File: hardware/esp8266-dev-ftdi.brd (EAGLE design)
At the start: 100 x 80 mm, 28 parts, among them CON1 USBMICRO-NO_CENTER, IC2 3V3

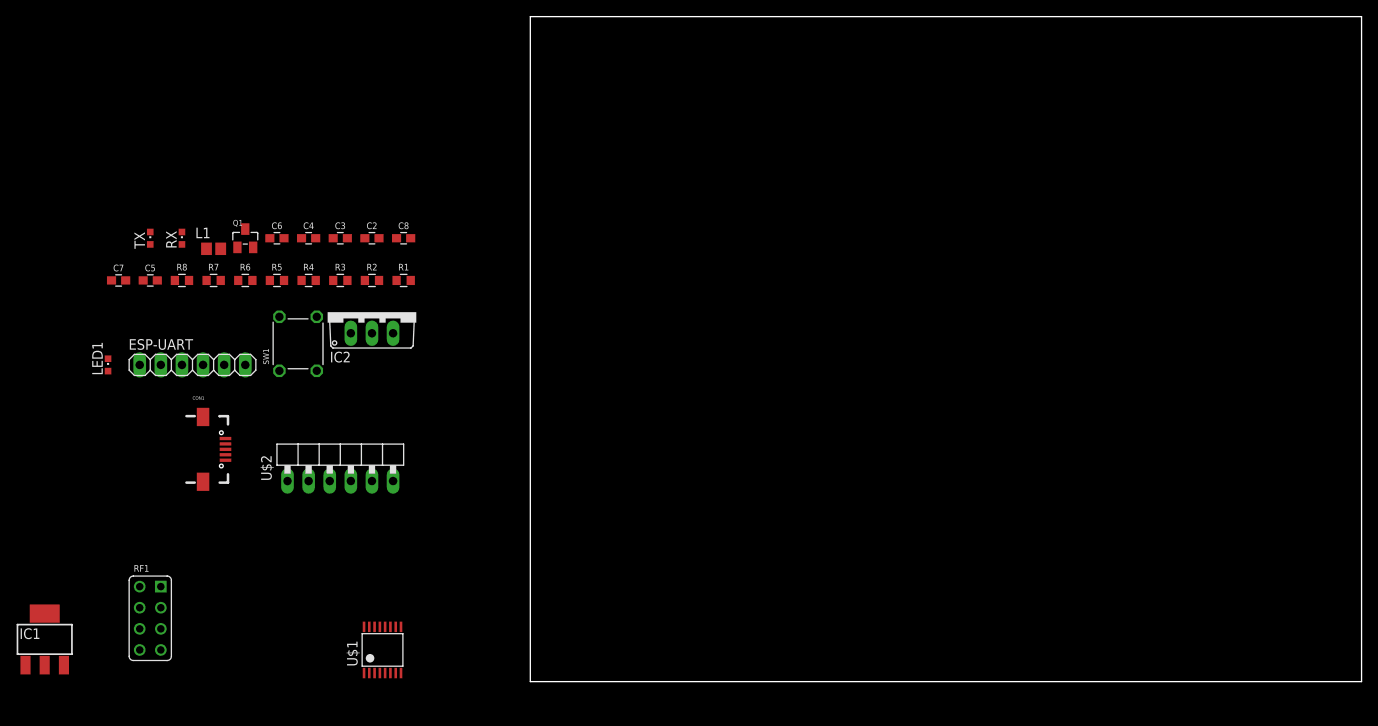
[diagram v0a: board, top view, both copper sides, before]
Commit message: Added LEDs
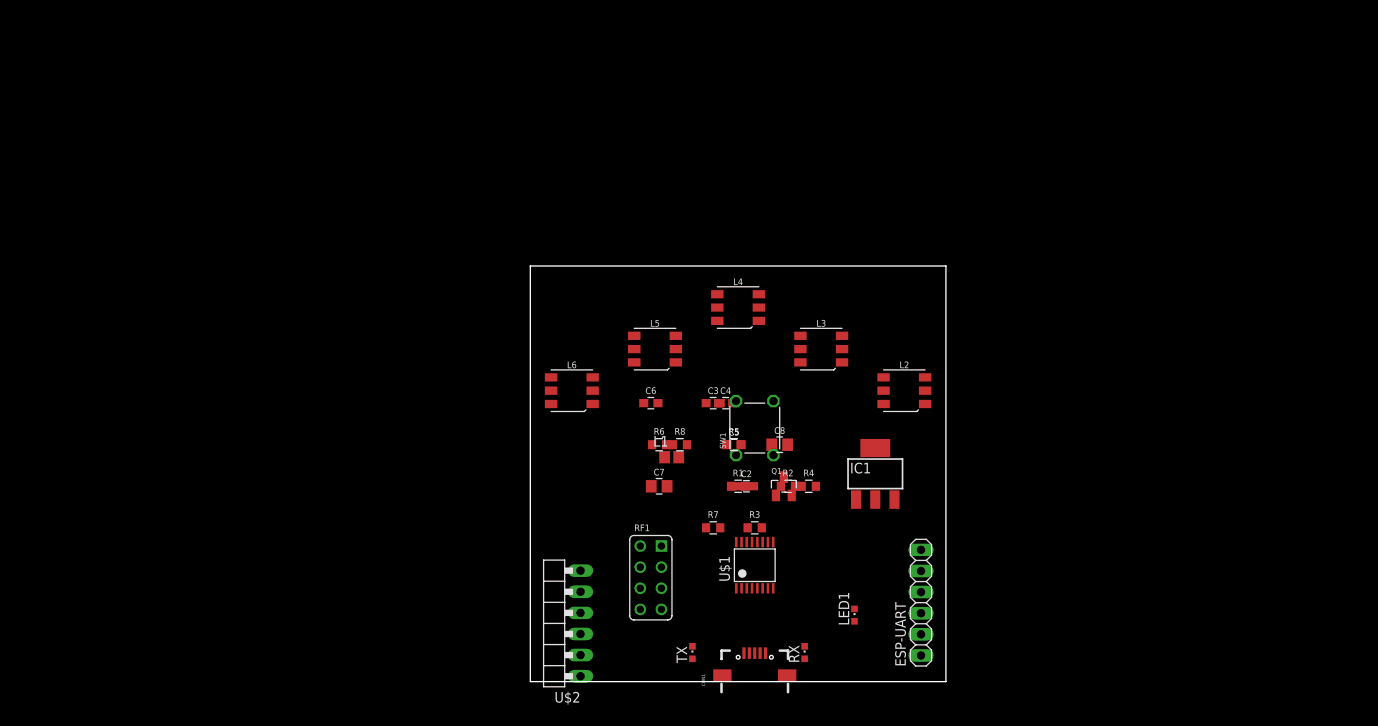
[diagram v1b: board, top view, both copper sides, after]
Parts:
- removed IC2: 3V3, p.peter-regulators:TO220V
- added L2, L3, L4, L5, L6: WS2812S, p.peter-leds:CHIP-5050
- C7: value 330n -> 10u; device p.peter-rcl:C0603 -> p.peter-rcl:C0805
- C8: value 100n -> 22u; device p.peter-rcl:C0603 -> p.peter-rcl:C0805
- moved IC1 101.9 mm to (41.5, 25.0)
- moved LED1 94.7 mm to (39.0, 8.00)
- moved ESP-UART 92.2 mm to (47.0, 9.50), turned to 90 degrees
- moved RX 90.0 mm to (33.0, 3.50)
- moved TX 82.1 mm to (19.5, 3.50)
- moved C5 72.9 mm to (24.5, 28.5)
- moved Q1 71.3 mm to (30.5, 23.5)
- moved CON1 70.1 mm to (27.0, 2.00), turned to 90 degrees
- moved C7 69.6 mm to (15.5, 23.5)
- moved R7 67.1 mm to (22.0, 18.5)
- moved R4 65.1 mm to (33.5, 23.5)
- moved R8 63.1 mm to (18.0, 28.5)
- moved L1 60.5 mm to (17.0, 27.0)
- moved RF1 60.4 mm to (14.5, 12.5)
- moved R5 58.4 mm to (24.5, 28.5)
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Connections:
- net +3V3: now also IC1.2, IC1.4; no longer IC2.3
- net +5V: now also IC1.3; no longer IC2.1
- net GND: now also IC1.1; no longer IC2.2
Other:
- board size 100 x 80 mm -> 50 x 50 mm

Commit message: schematic mostly done
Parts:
- removed ESP-UART: (no value), p.peter-connectors:PINHEADER-100MIL-1X6
- removed L2, L3, L4, L5, L6: WS2812S, p.peter-leds:CHIP-5050
- removed RX, TX: (no value), p.peter-leds:CHIPLED_0603
- added F1: 500mA, p.peter-regulators:SMD-FUSE-0805
- added LED-RX, LED-TX: (no value), p.peter-leds:CHIPLED_0805
- added LED2, LED3, LED4, LED5, LED6: (no value), p.peter-leds:CHIP-5050-4_PIN
- added R10, R9: 2k, p.peter-rcl:R0603
- added SJ1: (no value), jumper:SJ
- added SJ2: (no value), jumper:SJ_2
- added SW2, SW3, SW4: (no value), p.peter-passives:SWITCH-GENERIC-2_PIN
- L1: value (none) -> 875-MI0805K601R-10; device dp_devices:FB603 -> p.peter-passives:R0805
- LED1: device p.peter-leds:CHIPLED_0603 -> p.peter-leds:CHIPLED_0805
- moved U$2 20.0 mm to (4.00, 27.0)
- moved RF1 9.19 mm to (18.0, 21.0), turned to 45 degrees
- moved C4 0.71 mm to (24.0, 34.0)
- moved C5 0.71 mm to (25.0, 29.0)
- moved C6 0.71 mm to (15.0, 34.0)
- moved C7 0.71 mm to (16.0, 24.0)
- moved Q1 0.71 mm to (31.0, 24.0)
- moved R4 0.71 mm to (34.0, 24.0)
- moved R5 0.71 mm to (25.0, 29.0)
- moved R6 0.71 mm to (16.0, 29.0)
- moved C2 0.50 mm to (26.0, 24.0)
- moved C3 0.50 mm to (22.0, 34.0)
- moved C8 0.50 mm to (30.0, 29.0)
- moved IC1 0.50 mm to (42.0, 25.0)
- moved R1 0.50 mm to (25.0, 24.0)
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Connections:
- new net N$12: LED2.P$2, LED3.P$4
- new net N$15: LED3.P$2, LED4.P$4
- new net N$16: LED4.P$2, LED5.P$4
- new net N$17: LED5.P$2, LED6.P$4
- new net N$18: CON1.VUSB, F1.2, SJ1.2
- new net N$20: R9.2, SW3.P$1
- new net N$21: R10.2, SW4.P$1
- new net VCCIO: SJ2.2, U$1.3, U$2.3
- net +3V3: now also SJ2.3; no longer ESP-UART.3, U$1.3
- net +5V: now also LED2.P$1, LED3.P$1, LED4.P$1, LED5.P$1, LED6.P$1, SJ2.1; no longer U$2.3
- net /SLEEP: now also U$2.6
- net CTS: now also U$2.2
- net GND: now also LED-RX.C, LED-TX.C, LED2.P$3, LED3.P$3, LED4.P$3, LED5.P$3, LED6.P$3, R10.1, R9.1, SW2.P$1; no longer ESP-UART.1, RX.C, TX.C
- net IO2: now also LED2.P$4
- net N$10: now also SW2.P$2
- net N$2: now also F1.1, SJ1.1; no longer CON1.VUSB
- net N$3: now also LED-TX.A; no longer TX.A
- net N$8: now also LED-RX.A; no longer RX.A
- net RX: now also SW4.P$2; no longer ESP-UART.5
- net TX: now also SW3.P$2; no longer ESP-UART.4

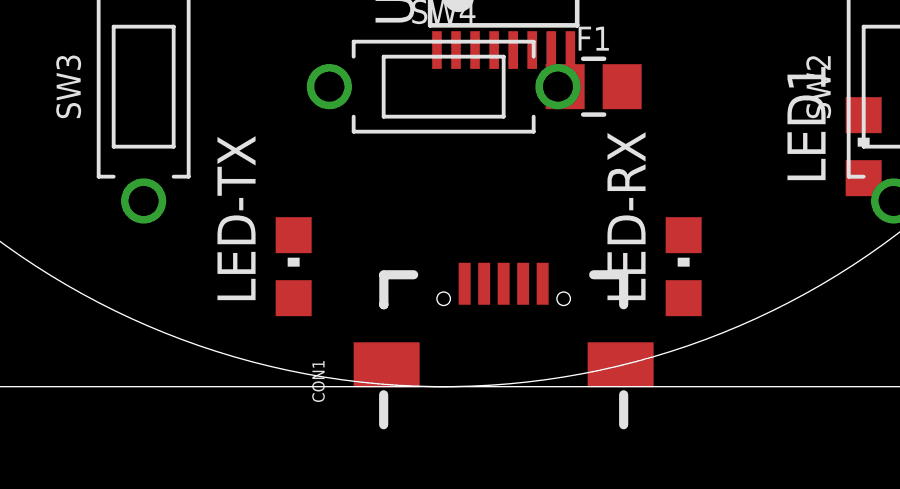
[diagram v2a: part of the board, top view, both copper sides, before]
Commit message: new USB connector with longer pads
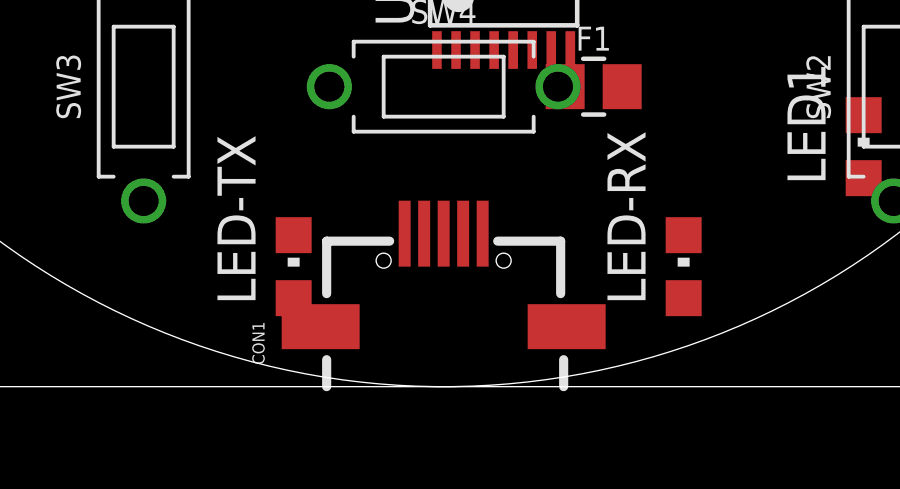
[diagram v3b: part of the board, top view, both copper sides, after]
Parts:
- CON1: value USBMICRO-NO_CENTER -> USBMICRO-NO_CENTER-LONG_PADS; device p.peter-connectors:USB-MICRO-SMD-NO_CENTER -> p.peter-connectors:USB-MICRO-SMD-NO_CENTER-LONG_PADS
- moved CON1 2.00 mm to (25.0, 2.00)
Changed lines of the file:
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@@
 <setting verticaltext="up"/>
 </settings>
-<grid distance="5" unitdist="mm" unit="mm" style="dots" multiple="1" display="no" altdistance="1" altunitdist="mm" altunit="mm"/>
+<grid distance="1" unitdist="mm" unit="mm" style="dots" multiple="1" display="yes" altdistance="0.1" altunitdist="mm" altunit="mm"/>
 <layers>
 <layer number="1" name="Top" color="4" fill="1" visible="yes" active="yes"/>
@@
 <element name="C7" library="p.peter-rcl" package="C0805" value="10u" x="16" y="24"/>
 <element name="C8" library="p.peter-rcl" package="C0805" value="22u" x="30" y="29"/>
-<element name="CON1" library="p.peter-connectors" package="USB-MICRO-SMD-NO_CENTER" value="USBMICRO-NO_CENTER" x="27" y="2" rot="R90"/>
+<element name="CON1" library="p.peter-connectors" package="USB-MICRO-SMD-NO_CENTER-LONG_PADS" value="USBMICRO-NO_CENTER-LONG_PADS" x="25" y="2" rot="R90"/>
 <element name="L1" library="p.peter-passives" package="R0805" value=" 875-MI0805K601R-10" x="17" y="27"/>
 <element name="LED1" library="p.peter-leds" package="CHIPLED_0805" value="" x="39" y="8"/>
@@
 <wire x1="6.54" y1="20.65" x2="7.7" y2="33.4" width="0" layer="19" extent="1-1"/>
 <wire x1="20" y1="5.05" x2="6.54" y2="20.65" width="0" layer="19" extent="1-1"/>
-<wire x1="28.3" y1="3.43" x2="20" y2="5.05" width="0" layer="19" extent="1-1"/>
-<wire x1="33" y1="5.05" x2="28.3" y2="3.43" width="0" layer="19" extent="1-1"/>
-<wire x1="27.317" y1="11.221" x2="28.3" y2="3.43" width="0" layer="19" extent="1-1"/>
+<wire x1="26.3" y1="5.1" x2="20" y2="5.05" width="0" layer="19" extent="1-1"/>
+<wire x1="33" y1="5.05" x2="26.3" y2="5.1" width="0" layer="19" extent="1-1"/>
+<wire x1="27.317" y1="11.221" x2="26.3" y2="5.1" width="0" layer="19" extent="1-1"/>
 <wire x1="26.682" y1="16.779" x2="27.317" y2="11.221" width="0" layer="19" extent="1-1"/>
 <wire x1="26.85" y1="24" x2="26.682" y2="16.779" width="0" layer="19" extent="1-1"/>
@@
 <contactref element="C3" pad="1"/>
 <wire x1="21.15" y1="34" x2="25.85" y2="24" width="0" layer="19" extent="1-1"/>
-<wire x1="26.35" y1="3.43" x2="21.15" y2="34" width="0" layer="19" extent="1-1"/>
+<wire x1="24.35" y1="5.1" x2="21.15" y2="34" width="0" layer="19" extent="1-1"/>
 </signal>
 <signal name="N$5">
@@
 <contactref element="C4" pad="1"/>
 <wire x1="23.15" y1="34" x2="31.85" y2="24" width="0" layer="19" extent="1-1"/>
-<wire x1="27" y1="3.43" x2="23.15" y2="34" width="0" layer="19" extent="1-1"/>
+<wire x1="25" y1="5.1" x2="23.15" y2="34" width="0" layer="19" extent="1-1"/>
 </signal>
 <signal name="TX">
@@
 <contactref element="SJ1" pad="2"/>
 <wire x1="30.95" y1="10" x2="35.762" y2="20" width="0" layer="19" extent="1-1"/>
-<wire x1="25.7" y1="3.43" x2="30.95" y2="10" width="0" layer="19" extent="1-1"/>
+<wire x1="23.7" y1="5.1" x2="30.95" y2="10" width="0" layer="19" extent="1-1"/>
 </signal>
 <signal name="N$20">

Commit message: starting layout
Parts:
- added JP1: (no value), pinhead:2X05
- added R11: 10k, p.peter-rcl:R0603
- added TP1, TP10, TP11, TP2, TP3, TP4, TP5, TP6, TP7, TP8, TP9: TPSQTP15R, testpad:TP15R
- moved SW3 30.9 mm to (43.0, 23.0)
- moved SW1 23.9 mm to (14.0, 11.0)
- moved RF1 14.3 mm to (32.0, 18.0), turned to 135 degrees
- moved U$2 2.24 mm to (3.00, 25.0)
- moved CON1 0.50 mm to (25.0, 2.50)
- flipped C2 to the bottom
- flipped C3 to the bottom
- flipped C4 to the bottom
- flipped C5 to the bottom
- flipped C6 to the bottom
- flipped C7 to the bottom
- flipped C8 to the bottom
- flipped F1 to the bottom
- flipped IC1 to the bottom
- flipped L1 to the bottom
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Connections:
- removed net N$10: Q1.P$3, R6.1, RF1.H_PD, SW2.P$2
- new net RESET: JP1.9, Q1.P$3, R6.1, RF1.H_PD, SW2.P$2, TP5.TP
- net +3V3: now also JP1.3, R11.1, TP10.TP
- net +5V: now also JP1.1, TP9.TP
- net /PWREN: now also TP7.TP
- net /SLEEP: now also TP6.TP
- net CTS: now also TP2.TP
- net GND: now also JP1.4, TP11.TP
- net IO0: now also JP1.6
- net IO16: now also JP1.10
- net IO2: now also JP1.8, R11.2
- net RTS: now also TP1.TP
- net RX: now also JP1.5, TP3.TP
- net TX: now also JP1.7, TP4.TP
- net VCCIO: now also JP1.2, TP8.TP
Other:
- outline, holes or cut-outs redrawn

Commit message: board outline and orga
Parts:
- removed SW4: (no value), p.peter-passives:SWITCH-GENERIC-2_PIN
- added SW-RESET: (no value), p.peter-passives:SWITCH-GENERIC-2_PIN
- moved SW3 36.8 mm to (9.00, 9.00), turned to 315 degrees
- moved JP1 26.2 mm to (46.0, 25.0), flipped to the bottom
- moved SW1 5.39 mm to (16.0, 16.0), turned to 45 degrees
- moved LED2 5.00 mm to (9.00, 38.0), turned to 45 degrees
- moved LED6 5.00 mm to (41.0, 38.0), turned to 315 degrees
- moved LED3 3.16 mm to (16.0, 44.0), turned to 22.5 degrees
- moved LED5 2.24 mm to (34.0, 44.0), turned to 337.5 degrees
- moved LED4 2.00 mm to (25.0, 46.0)
- moved SW2 1.41 mm to (41.0, 9.00), turned to 225 degrees
- moved U$2 1.00 mm to (2.00, 25.0), flipped to the bottom, turned to 270 degrees
- moved RF1 0.42 mm to (31.7, 18.3)
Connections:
- net GND: now also SW-RESET.P$1; no longer SW2.P$1
- net N$20: now also SW2.P$1; no longer SW3.P$1
- net N$21: now also SW3.P$1; no longer SW4.P$1
- net RESET: now also SW-RESET.P$2; no longer SW2.P$2
- net RX: now also SW3.P$2; no longer SW4.P$2
- net TX: now also SW2.P$2; no longer SW3.P$2
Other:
- outline, holes or cut-outs redrawn

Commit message: LED power
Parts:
- removed TP1, TP10, TP11, TP2, TP3, TP4, TP5, TP6, TP7, TP8, TP9: TPSQTP15R, testpad:TP15R
- C2, C3, C4, C5, C6: device p.peter-rcl:C0603 -> p.peter-rcl:C0805
- R1, R10, R11, R2, R3, R4, R5, R6, R7, R8, R9: device p.peter-rcl:R0603 -> p.peter-rcl:R0805
- moved LED-RX 32.6 mm to (9.00, 26.0), flipped to the top, turned to 270 degrees
- moved LED2 32.5 mm to (41.5, 38.5), turned to 315 degrees
- moved LED6 32.5 mm to (8.50, 38.5), turned to 45 degrees
- moved IC1 30.2 mm to (17.0, 8.00), turned to 180 degrees
- moved LED-TX 30.1 mm to (9.00, 32.0), flipped to the top, turned to 90 degrees
- moved R10 28.9 mm to (23.0, 43.0)
- moved SJ2 28.0 mm to (14.0, 43.0)
- moved R9 27.3 mm to (34.0, 42.0)
- moved R7 27.0 mm to (22.0, 46.0)
- moved C8 25.8 mm to (12.4, 10.2), turned to 270 degrees
- moved SW1 25.5 mm to (34.0, 34.0)
- moved R3 25.1 mm to (39.0, 41.0)
- moved R11 24.2 mm to (10.0, 38.0)
- moved R4 22.1 mm to (27.0, 45.0)
- moved SW-RESET 21.2 mm to (18.0, 18.0)
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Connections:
- net +3V3: no longer TP10.TP
- net +5V: no longer TP9.TP
- net /PWREN: no longer TP7.TP
- net /SLEEP: no longer TP6.TP
- net CTS: no longer TP2.TP
- net GND: no longer TP11.TP
- net RESET: no longer TP5.TP
- net RTS: no longer TP1.TP
- net RX: no longer TP3.TP
- net TX: no longer TP4.TP
- net VCCIO: no longer TP8.TP
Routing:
- net +5V: track 0.00 -> 77.1 mm, vias 0 -> 2
- net GND: track 0.00 -> 45.3 mm, vias 0 -> 1
- net N$4: track 0.00 -> 17.6 mm, vias 0 -> 1
- net N$7: track 0.00 -> 17.0 mm, vias 0 -> 1
- net +3V3: track 0.00 -> 10.8 mm
- net N$18: track 0.00 -> 9.79 mm, vias 0 -> 1
- net N$2: track 0.00 -> 9.25 mm
- net N$12: track 0.00 -> 5.73 mm
- net N$15: track 0.00 -> 5.69 mm
- net N$16: track 0.00 -> 5.53 mm
- net N$17: track 0.00 -> 4.86 mm
- net N$6: track 0.00 -> 2.28 mm
- net N$5: track 0.00 -> 2.28 mm
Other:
- outline, holes or cut-outs redrawn

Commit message: Everything routed
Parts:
- JP1: device pinhead:2X05 -> p.peter-connectors:PINHEADER-100MIL-2X5-NOSILK
- moved R9 36.6 mm to (33.4, 5.40), turned to 180 degrees
- moved R10 35.2 mm to (10.2, 10.2), turned to 270 degrees
- moved R3 34.9 mm to (8.60, 23.8), turned to 180 degrees
- moved R6 33.7 mm to (30.8, 9.80), turned to 270 degrees
- moved R4 30.1 mm to (8.60, 21.2), turned to 180 degrees
- moved Q1 28.7 mm to (33.6, 10.0)
- moved SJ2 28.5 mm to (37.2, 26.4), turned to 270 degrees
- moved R8 28.5 mm to (33.6, 13.2), turned to 180 degrees
- moved R11 24.9 mm to (29.6, 22.6), turned to 270 degrees
- moved R7 22.6 mm to (38.4, 30.4)
- moved C5 16.5 mm to (18.4, 27.0), turned to 90 degrees
- moved C6 11.5 mm to (16.2, 27.0), turned to 90 degrees
- moved LED-TX 8.21 mm to (8.60, 23.8), turned to 270 degrees
- moved LED-RX 4.82 mm to (8.60, 21.2)
- moved LED1 0.20 mm to (28.6, 7.40)
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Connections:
- net +5V: now also JP1.10; no longer JP1.1
- net /PWREN: now also U$1.7; no longer U$1.16
- net /SLEEP: now also U$1.16; no longer U$1.15
- net GND: now also JP1.9; no longer JP1.4
- net IO16: now also JP1.1; no longer JP1.10
- net N$13: now also U$1.15; no longer U$1.7
- net RESET: now also JP1.2; no longer JP1.9
- net RX: now also JP1.4; no longer JP1.5
- net TX: now also JP1.5; no longer JP1.7
- net VCCIO: now also JP1.7; no longer JP1.2
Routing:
- net GND: track 45.3 -> 198.3 mm, vias 1 -> 5
- net TX: track 0.00 -> 80.2 mm, vias 0 -> 1
- net RX: track 0.00 -> 77.2 mm, vias 0 -> 1
- net +3V3: track 10.8 -> 78.3 mm, vias 0 -> 1
- net +5V: track 77.1 -> 132.5 mm, vias 2 -> 4
- net VCCIO: track 0.00 -> 52.1 mm
- net RESET: track 0.00 -> 39.8 mm
- net IO2: track 0.00 -> 38.9 mm, vias 0 -> 3
- net IO0: track 0.00 -> 28.7 mm, vias 0 -> 3
- net /SLEEP: track 0.00 -> 27.8 mm
- net CTS: track 0.00 -> 27.6 mm, vias 0 -> 2
- net /PWREN: track 0.00 -> 19.4 mm
- net N$14: track 0.00 -> 19.2 mm
- net N$13: track 0.00 -> 17.3 mm
- net IO16: track 0.00 -> 13.0 mm
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
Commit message: Layout done
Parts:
- removed SW3: (no value), p.peter-passives:SWITCH-GENERIC-2_PIN
- removed U$1: FTDI-FT230XSSOP16, p.peter-ics:SSOP-16-FTDI
- added FLASH: (no value), p.peter-passives:SWITCH-GENERIC-4_PIN
- added FT230: FTDI-FT230XSSOP16, p.peter-ics:SSOP-16-FTDI
- added SLEEP: (no value), jumper:SJ
- added U$3: (no value), p.peter-doc:LOGO-JUSTGEEK-XS
- RF1: device p.peter-periphery:ESP8266-ESP-01-NOSILK -> p.peter-periphery:ESP8266-ESP-01
- SW1: device p.peter-passives:SWITCH-GENERIC-4_PIN -> p.peter-passives:SWITCH-GENERIC-2_PIN
- moved SW1 35.4 mm to (9.00, 9.00), turned to 135 degrees
- moved LED1 1.61 mm to (27.8, 8.80), turned to 180 degrees
- moved Q1 1.00 mm to (34.6, 10.0)
- moved R8 1.00 mm to (34.6, 13.2)
- moved R9 1.00 mm to (34.4, 5.40)
- moved R6 0.80 mm to (31.6, 9.80)
- moved R5 0.60 mm to (29.2, 9.80)
- moved R10 0.40 mm to (9.80, 10.2)
- moved C8 0.20 mm to (12.2, 10.2)
- moved F1 0.20 mm to (23.0, 6.20)
- renumbered SW-RESET to RESET
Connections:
- new net N$10: SLEEP.2, U$2.6
- net +5V: now also FT230.11, FT230.12; no longer U$1.11, U$1.12
- net /PWREN: now also FT230.7; no longer U$1.7
- net /SLEEP: now also FT230.16, SLEEP.1; no longer U$1.16, U$2.6
- net CTS: now also FT230.6; no longer U$1.6
- net GND: now also FLASH.P$3, FLASH.P$4, FT230.13, FT230.5; no longer SW1.P$3, SW1.P$4, U$1.13, U$1.5
- net N$11: now also FLASH.P$1, FLASH.P$2; no longer SW1.P$1, SW1.P$2
- net N$13: now also FT230.15; no longer U$1.15
- net N$14: now also FT230.14; no longer U$1.14
- net N$21: now also SW1.P$1; no longer SW3.P$1
- net N$5: now also FT230.9; no longer U$1.9
- net N$6: now also FT230.8; no longer U$1.8
- net RTS: now also FT230.2; no longer U$1.2
- net RX: now also FT230.4, SW1.P$2; no longer SW3.P$2, U$1.4
- net TX: now also FT230.1; no longer U$1.1
- net VCCIO: now also FT230.3; no longer U$1.3
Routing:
- net N$9: track 0.00 -> 4.52 mm, vias 0 -> 1
- net +3V3: track 78.3 -> 82.5 mm
- net VCCIO: track 52.1 -> 55.9 mm
- net /PWREN: track 19.4 -> 23.0 mm
- net GND: track 198.3 -> 201.7 mm
- net N$10: track 0.00 -> 2.68 mm
- net RESET: track 39.8 -> 41.9 mm
- net /SLEEP: track 27.8 -> 26.3 mm
- net RX: track 77.2 -> 78.2 mm
- net N$20: track 4.33 -> 3.33 mm
- net N$6: track 2.28 -> 3.25 mm
- net N$5: track 2.28 -> 3.25 mm
- net +5V: track 132.5 -> 133.4 mm
- net CTS: track 27.6 -> 28.3 mm
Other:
- board text added: "0"
- board text added: "16"
- board text added: "2"
- board text added: "2015"
- board text added: "3V3"
- board text added: "5V"
- board text added: "ANY"
- board text added: "AWAY DAY"
- board text added: "CTS"
- board text added: "GND"
- board text added: "MAGIC GOES HERE"
- board text added: "RES"
- board text added: "RX"
- board text added: "SLEEP"
- board text added: "THING"
- board text added: "TX"
- board text added: "UART"
- board text added: "V+"
- board text added: "VCC"
